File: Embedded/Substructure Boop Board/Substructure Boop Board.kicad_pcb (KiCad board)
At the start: 2 copper layers, 30 x 40 mm, 41 parts, among them U1 PN5321A3HN_C1xx, U2 AD7142ACPZ-500RL7, U3 LD1117S33TR_SOT223, U4 0.35uH (Per Coil), U5 R FFC, Y1 7M-27.120MAAJ-T

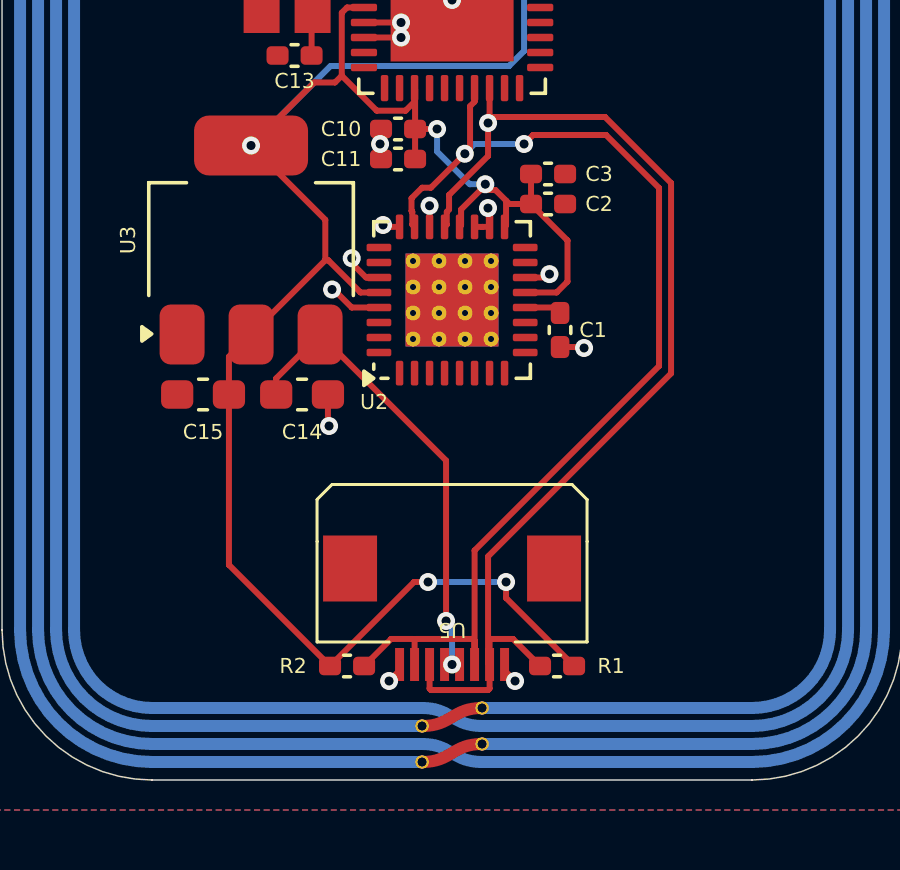
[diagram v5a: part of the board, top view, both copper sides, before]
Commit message: Added Keep Out Zones (Radio EMI Reduction)
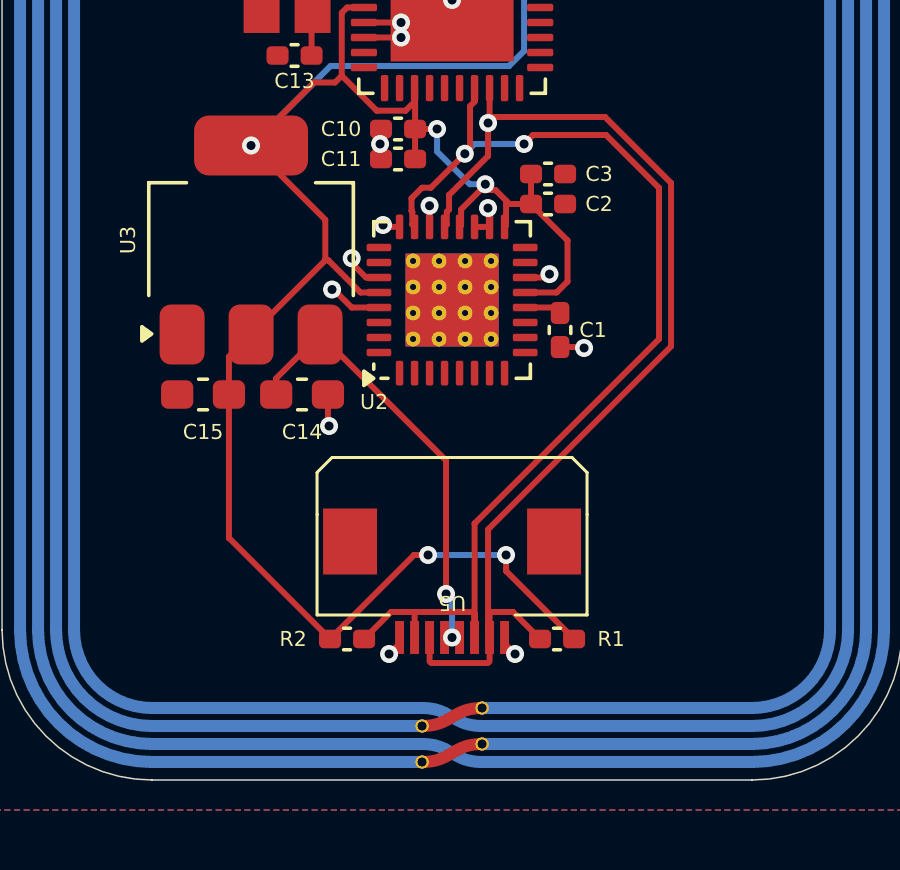
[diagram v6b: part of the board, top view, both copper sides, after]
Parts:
- moved R1 0.90 mm to (118.5, 85.3)
- moved R2 0.90 mm to (111.5, 85.3)
- moved U5 0.90 mm to (115.0, 84.6)
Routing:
- net I2C SDA: track 37.5 -> 36.4 mm
- net +3V3: track 80.0 -> 79.1 mm
- net +5V: track 15.9 -> 15.0 mm
- net I2C SCL: track 37.3 -> 36.4 mm

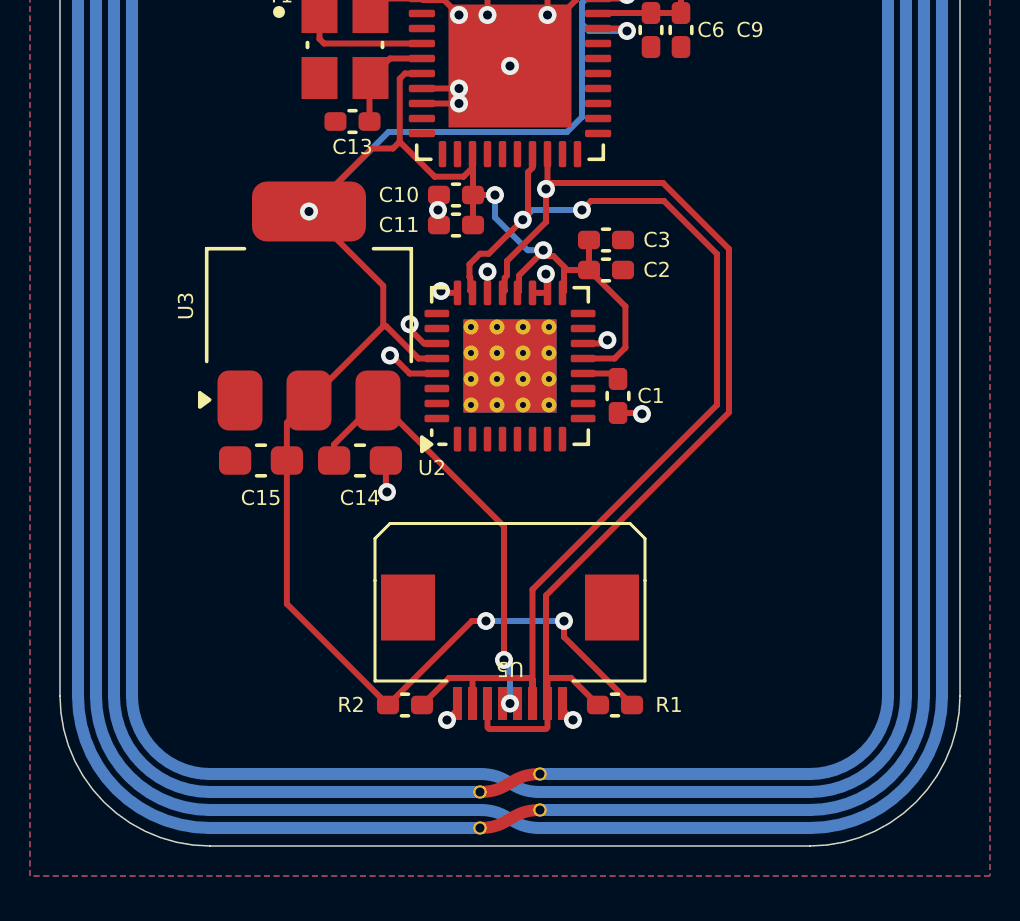
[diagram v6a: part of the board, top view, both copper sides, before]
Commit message: Added Capacitive sensor pads
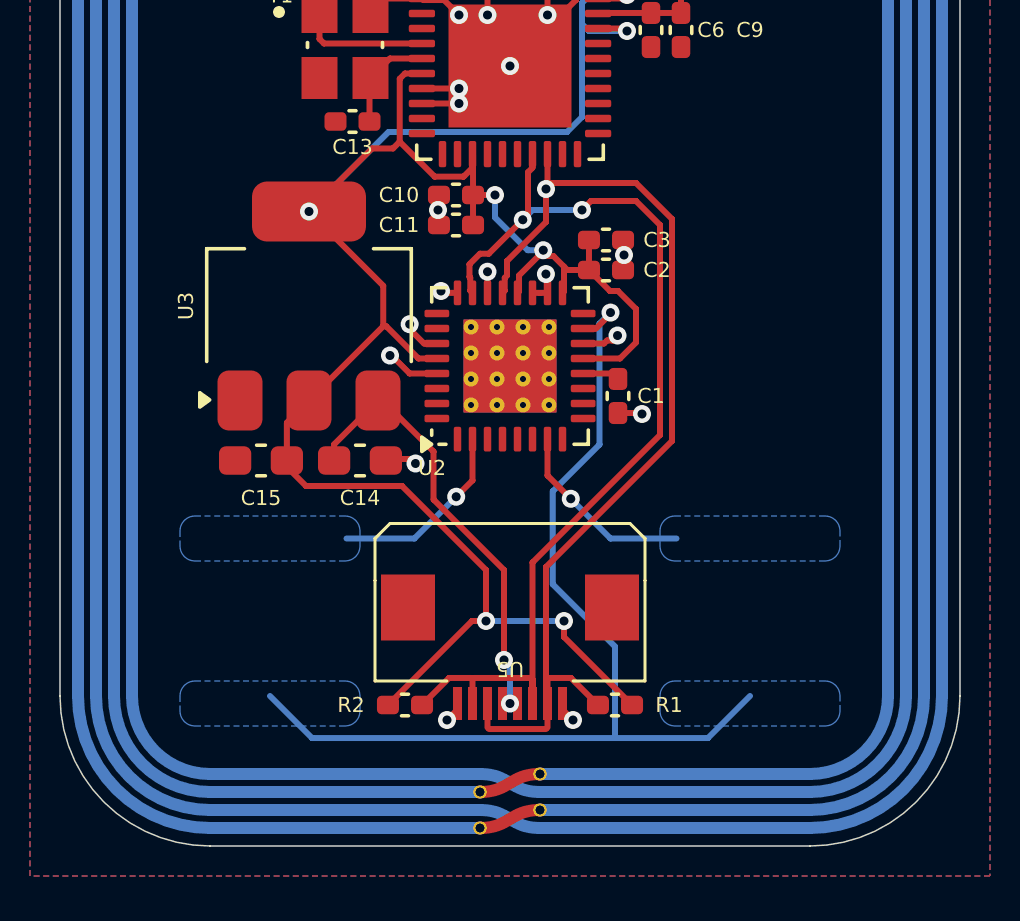
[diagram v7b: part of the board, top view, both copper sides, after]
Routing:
- net unconnected-(U2-SRC-Pad15): track 0.00 -> 34.2 mm, vias 0 -> 1
- net unconnected-(U2-CIN9-Pad7): track 0.00 -> 6.38 mm, vias 0 -> 1
- net unconnected-(U2-CIN4-Pad2): track 0.00 -> 6.38 mm, vias 0 -> 1
- net I2C SCL: track 36.4 -> 34.3 mm
- net I2C SDA: track 36.4 -> 34.3 mm
- net +3V3: track 79.1 -> 80.1 mm
- net GND: track 58.3 -> 59.2 mm, vias 20 -> 21
- added copper zone on B.Cu, net unconnected-(U2-CIN4-Pad2)
- added copper zone on B.Cu, net unconnected-(U2-CIN9-Pad7)
- added copper zone on B.Cu, net unconnected-(U2-SRC-Pad15)

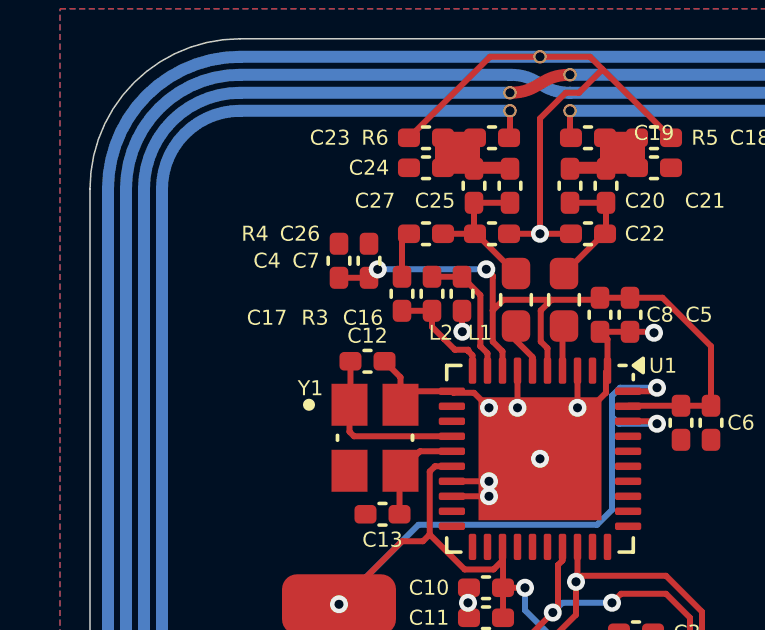
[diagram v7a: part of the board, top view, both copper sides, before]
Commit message: Added LCSC IDs
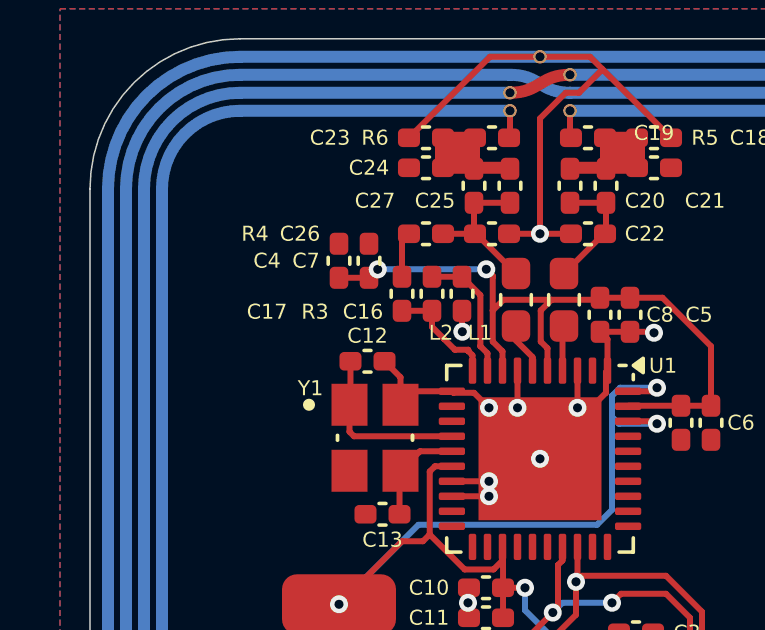
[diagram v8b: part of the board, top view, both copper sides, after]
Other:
- board text removed: "LEFT RIGHT"
